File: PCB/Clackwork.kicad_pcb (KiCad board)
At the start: 2 copper layers, 100 x 69.5 mm, 26 parts, among them J1 Conn_01x08_Pin, SW1 SW_Push_45deg, SW2 SW_Push_45deg, SW3 SW_Push_45deg, SW4 SW_Push_45deg, SW5 SW_Push_45deg, SW6 SW_Push_45deg, SW7 SW_Push_45deg, SW8 SW_Push_45deg, U1 XIAO-ESP32-C3-SMD

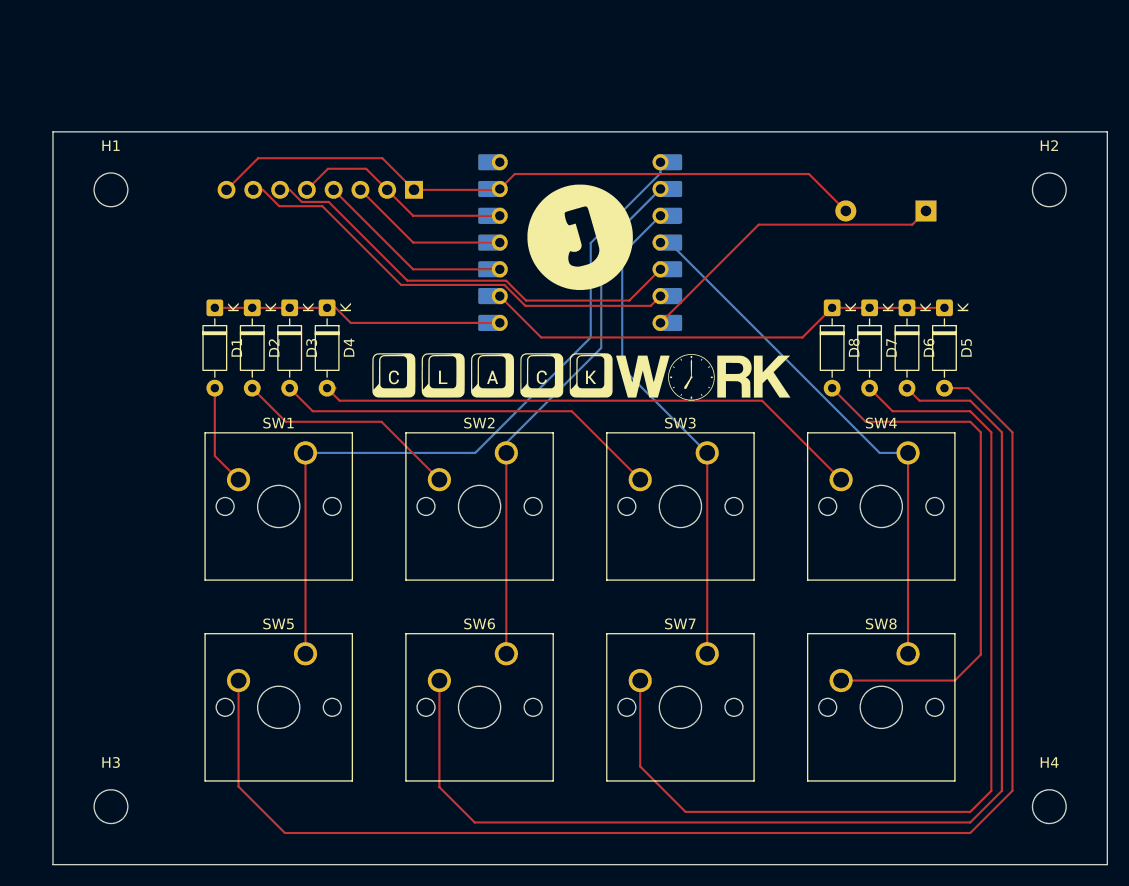
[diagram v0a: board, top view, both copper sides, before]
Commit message: Reworked PCB
All components on one side now, I shouldn't have followed the tutorial blindly
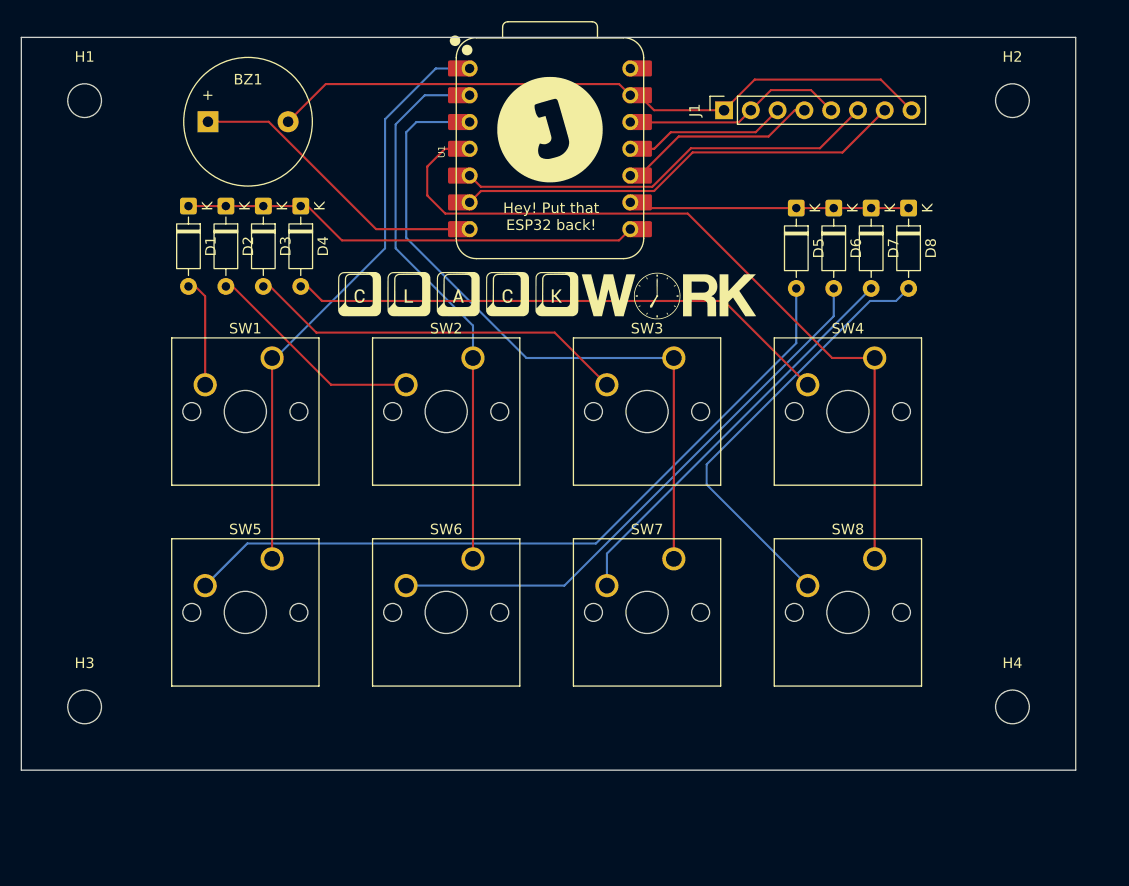
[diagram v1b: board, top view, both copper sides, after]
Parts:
- removed the G*** at (150.5, 87.0)
- removed the G*** at (150.5, 74.0)
- removed the G*** at (150.5, 127.0)
- added G***: LOGO, LOGO, F.Cu at (147.6, 63.8)
- added G***: LOGO, LOGO, F.Cu at (147.2, 79.2)
- added G***: LOGO, LOGO, B.Cu at (147.3, 117.2)
- BZ1, J1, U1: moved to F.Cu
- moved BZ1 68.6 mm to (115.2, 63.0), turned to 0 degrees
- moved J1 30.4 mm to (164.1, 61.9)
- moved D5 16.9 mm to (171.0, 71.2)
- moved D8 11.9 mm to (181.7, 71.2)
- moved D6 11.7 mm to (174.6, 71.2)
- moved H4 10.1 mm to (191.5, 118.5)
- moved D1 9.97 mm to (113.3, 71.0)
- moved D2 9.97 mm to (116.9, 71.0)
- moved D3 9.97 mm to (120.5, 71.0)
- moved D4 9.97 mm to (124.0, 71.0)
- moved H3 9.78 mm to (103.5, 118.5)
- moved SW3 9.54 mm to (159.4, 85.4)
- moved SW7 9.54 mm to (159.4, 104.5)
- moved SW1 9.54 mm to (121.3, 85.4)
- moved SW5 9.54 mm to (121.3, 104.5)
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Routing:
- net Net-(D5-A): track 129.1 -> 70.8 mm
- net Net-(D6-A): track 110.8 -> 53.8 mm
- net Net-(D7-A): track 91.4 -> 38.6 mm
- net COL3: track 50.0 -> 74.5 mm
- net ROW1: track 45.0 -> 25.8 mm
- net COL2: track 46.4 -> 65.6 mm
- net ROW0: track 27.6 -> 43.0 mm
- net COL0: track 70.0 -> 56.3 mm
- net Net-(D8-A): track 51.2 -> 41.5 mm
- net COL1: track 50.1 -> 52.4 mm
- net Net-(D4-A): track 53.2 -> 51.3 mm
- net /DC: track 41.7 -> 40.3 mm
- net Net-(BZ1-+): track 29.6 -> 28.2 mm
- net Net-(D3-A): track 36.8 -> 35.8 mm
- net Net-(D2-A): track 21.3 -> 20.3 mm
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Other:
- board text added: "Hey! Put that ESP32 back!"
